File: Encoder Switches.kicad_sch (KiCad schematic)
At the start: 0 parts

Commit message: Added oled hierarchical page and referenced other pages
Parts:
- added C? (x27): 100nf, symbol Device:C_Small
- added R? (x27): 10k, Resistor_SMD:R_0201_0603Metric, symbol Device:R
- added SW?: Encoder4, ksoloti_shield_footprints:ALPS_STEC12E08, symbol ksoloti_shield_symbols:RotaryEncoder_Switch_GND
- added SW?: Encoder3, ksoloti_shield_footprints:ALPS_STEC12E08, symbol ksoloti_shield_symbols:RotaryEncoder_Switch_GND
- added SW?: Encoder1, ksoloti_shield_footprints:ALPS_STEC12E08, symbol ksoloti_shield_symbols:RotaryEncoder_Switch_GND
- added SW?: Encoder7, ksoloti_shield_footprints:ALPS_STEC12E08, symbol ksoloti_shield_symbols:RotaryEncoder_Switch_GND
- added SW?: Encoder5, ksoloti_shield_footprints:ALPS_STEC12E08, symbol ksoloti_shield_symbols:RotaryEncoder_Switch_GND
- added SW?: Encoder8, ksoloti_shield_footprints:ALPS_STEC12E08, symbol ksoloti_shield_symbols:RotaryEncoder_Switch_GND
- added SW?: Encoder9, ksoloti_shield_footprints:ALPS_STEC12E08, symbol ksoloti_shield_symbols:RotaryEncoder_Switch_GND
- added SW?: Encoder6, ksoloti_shield_footprints:ALPS_STEC12E08, symbol ksoloti_shield_symbols:RotaryEncoder_Switch_GND
- added SW?: Encoder2, ksoloti_shield_footprints:ALPS_STEC12E08, symbol ksoloti_shield_symbols:RotaryEncoder_Switch_GND
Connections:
- new net: C?.1, R?.2, SW?.A (x9)
- new net +3.3V: R?.1, R?.1, R?.1, R?.1, R?.1, R?.1, R?.1, R?.1, R?.1, R?.1, R?.1, R?.1, R?.1, R?.1, R?.1, R?.1, R?.1, R?.1, R?.2, R?.2, R?.2, R?.2, R?.2, R?.2, R?.2, R?.2, R?.2
- new net ENC1_B: C?.1, R?.2, SW?.B
- new net ENC1_SW: C?.1, R?.1, SW?.S2
- new net ENC2_B: C?.1, R?.2, SW?.B
- new net ENC2_SW: C?.1, R?.1, SW?.S2
- new net ENC3_B: C?.1, R?.2, SW?.B
- new net ENC3_SW: C?.1, C?.1, R?.1, R?.1, SW?.S2, SW?.S2
- new net ENC4_B: C?.1, R?.2, SW?.B
- new net ENC4_SW: C?.1, R?.1, SW?.S2
- new net ENC5_B: C?.1, R?.2, SW?.B
- new net ENC5_SW: C?.1, R?.1, SW?.S2
- new net ENC6_B: C?.1, R?.2, SW?.B
- new net ENC6_SW: C?.1, R?.1, SW?.S2
- new net ENC7_B: C?.1, R?.2, SW?.B
- new net ENC8_B: C?.1, R?.2, SW?.B
- new net ENC8_SW: C?.1, R?.1, SW?.S2
- new net ENC9_B: C?.1, R?.2, SW?.B
- new net ENC9_SW: C?.1, R?.1, SW?.S2
- new net GND: C?.2, C?.2, C?.2, C?.2, C?.2, C?.2, C?.2, C?.2, C?.2, C?.2, C?.2, C?.2, C?.2, C?.2, C?.2, C?.2, C?.2, C?.2, C?.2, C?.2, C?.2, C?.2, C?.2, C?.2, C?.2, C?.2, C?.2, SW?.1, SW?.1, SW?.1, SW?.1, SW?.1, SW?.1, SW?.1, SW?.1, SW?.1, SW?.C, SW?.C, SW?.C, SW?.C, SW?.C, SW?.C, SW?.C, SW?.C, SW?.C, SW?.S1, SW?.S1, SW?.S1, SW?.S1, SW?.S1, SW?.S1, SW?.S1, SW?.S1, SW?.S1

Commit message: Annotated all components (numerating)
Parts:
- gave numbers to parts that had none: 63

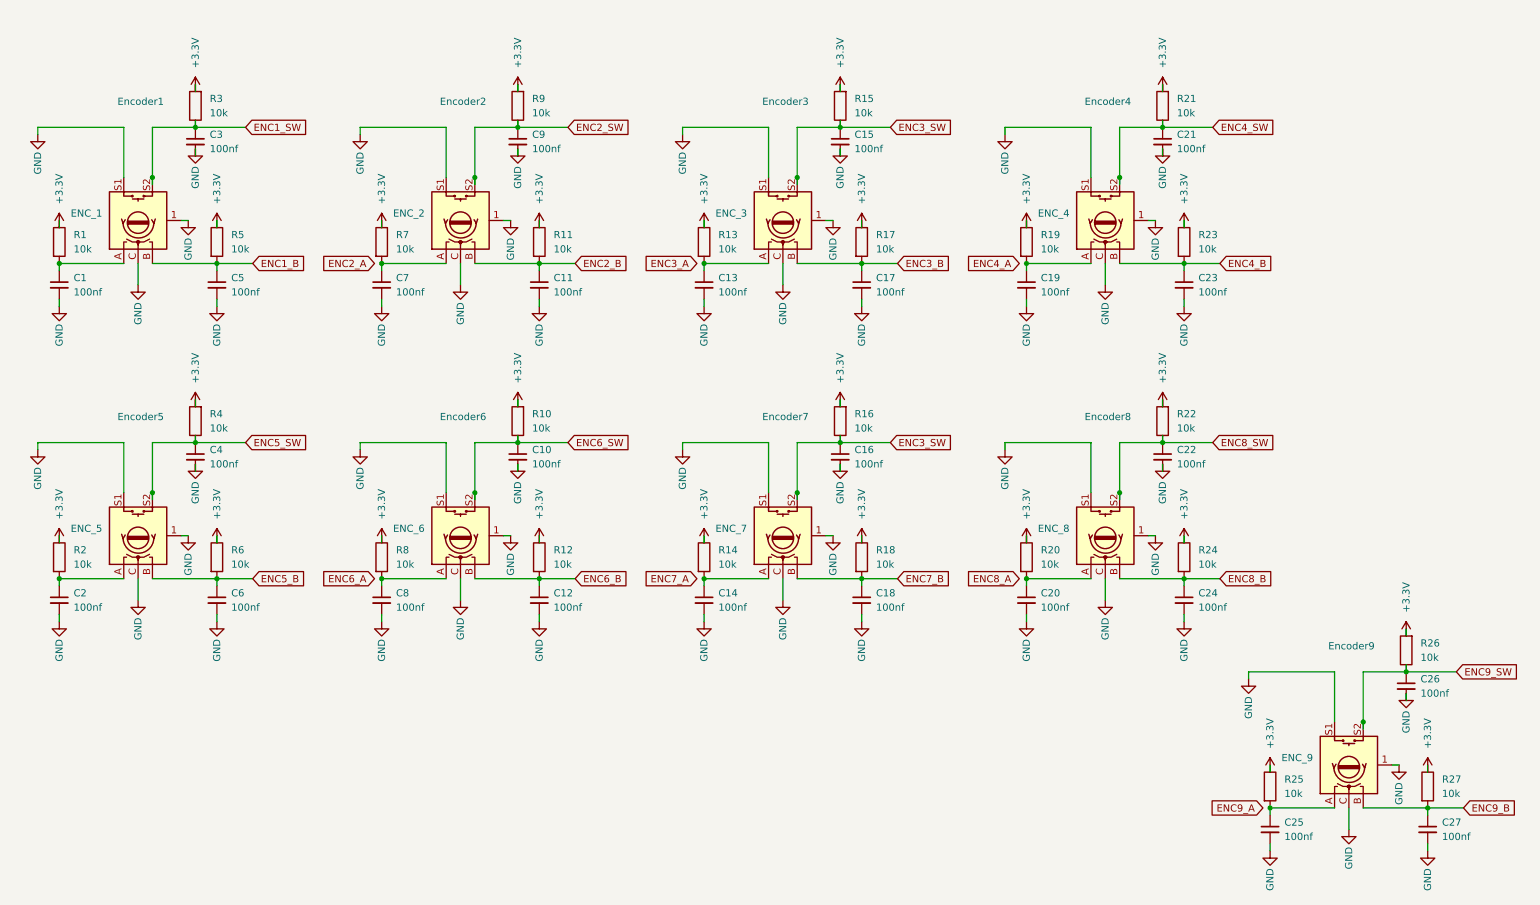
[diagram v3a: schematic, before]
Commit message: Cleaned up ERC errors
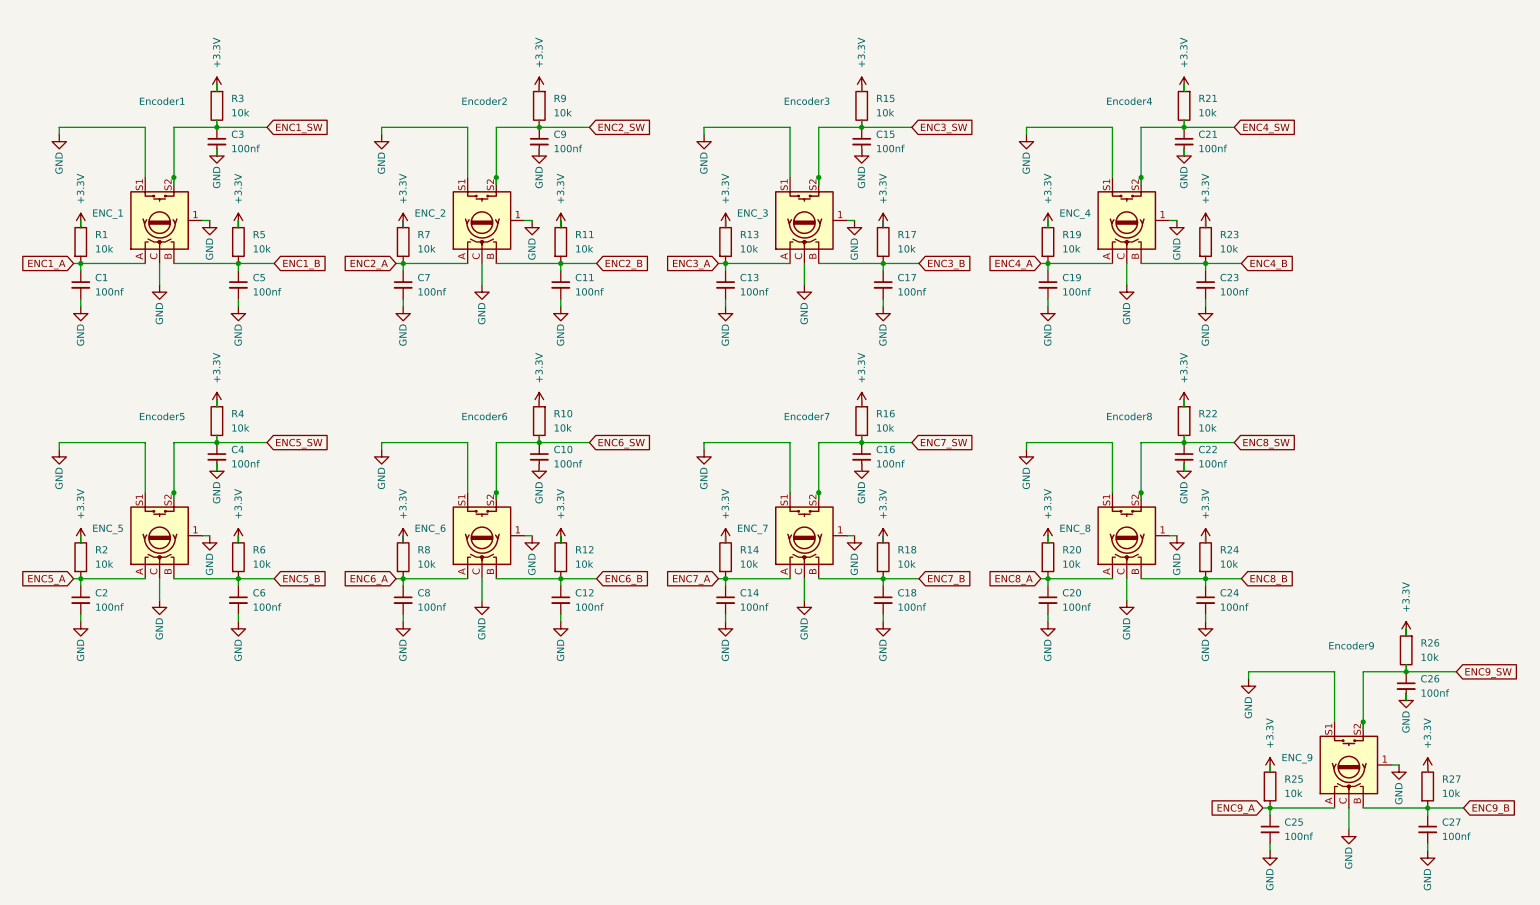
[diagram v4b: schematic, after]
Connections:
- net ENC2_A: now also C7.1, ENC_2.A, R7.2
- net ENC3_A: now also C13.1, ENC_3.A, R13.2
- net ENC3_SW: no longer C16.1, ENC_7.S2, R16.1
- net ENC4_A: now also C19.1, ENC_4.A, R19.2
- net ENC6_A: now also C8.1, ENC_6.A, R8.2
- net ENC7_A: now also C14.1, ENC_7.A, R14.2
- net ENC8_A: now also C20.1, ENC_8.A, R20.2
- net ENC9_A: now also C25.1, ENC_9.A, R25.2
- net ENC5_A: now reaches C2.1, ENC_5.A, R2.2
- net ENC1_A: now reaches C1.1, ENC_1.A, R1.2
- new net ENC7_SW: C16.1, ENC_7.S2, R16.1
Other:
- moved on the sheet: C1, C10, C11, C12, C13, C14, C15, C16, C17, C18, C19, C2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

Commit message: Solve all warnings
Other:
- moved on the sheet: R10, R15, R16, R21, R22, R26, R3, R4, R9

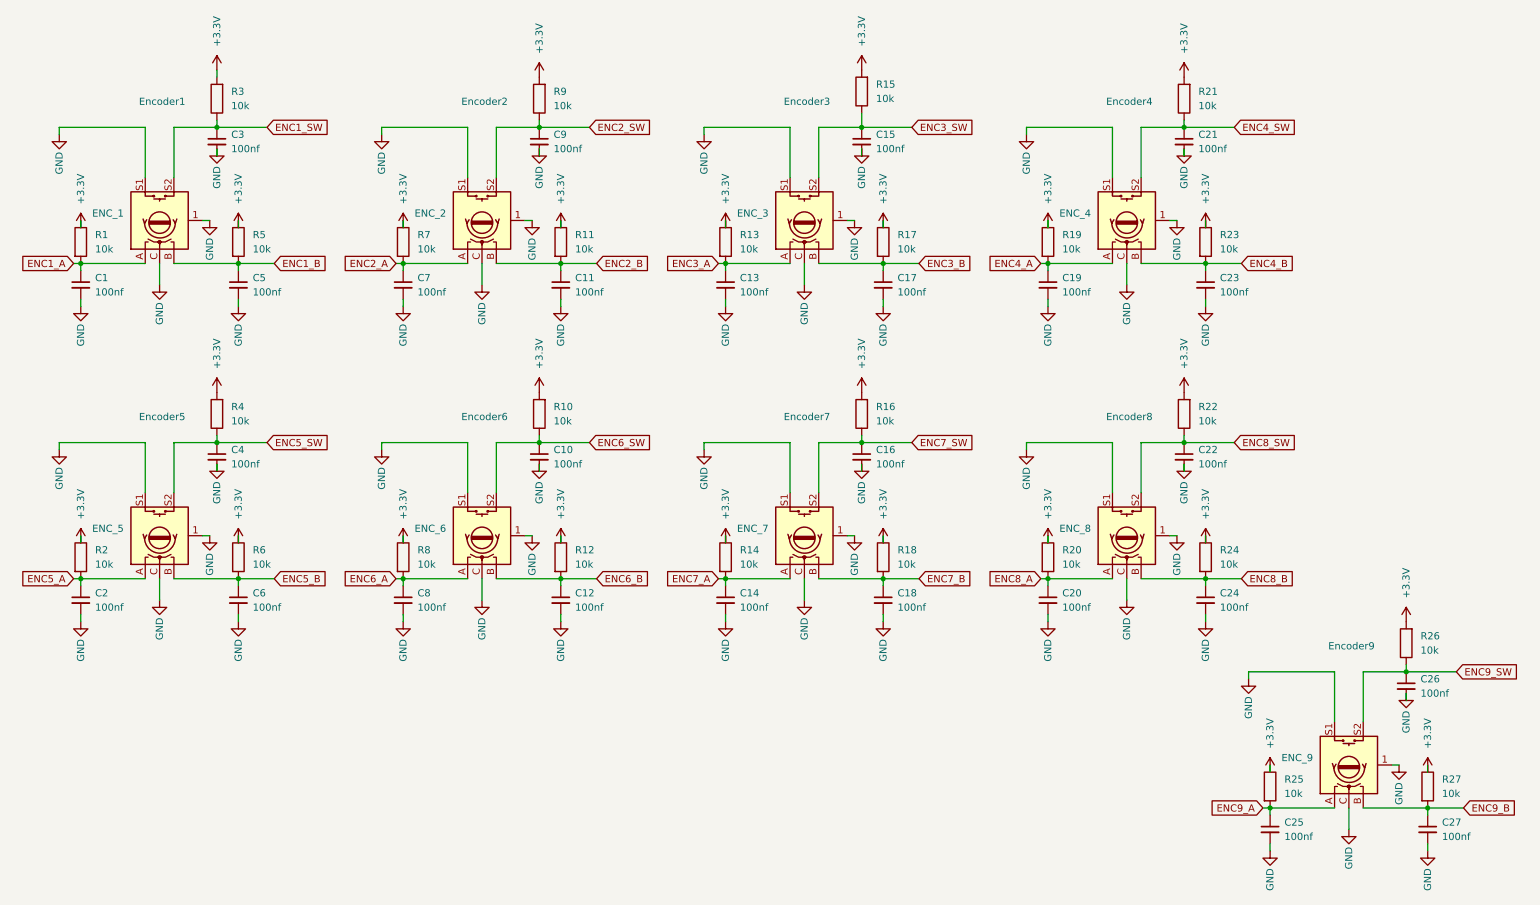
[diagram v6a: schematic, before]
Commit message: Removed final warnings
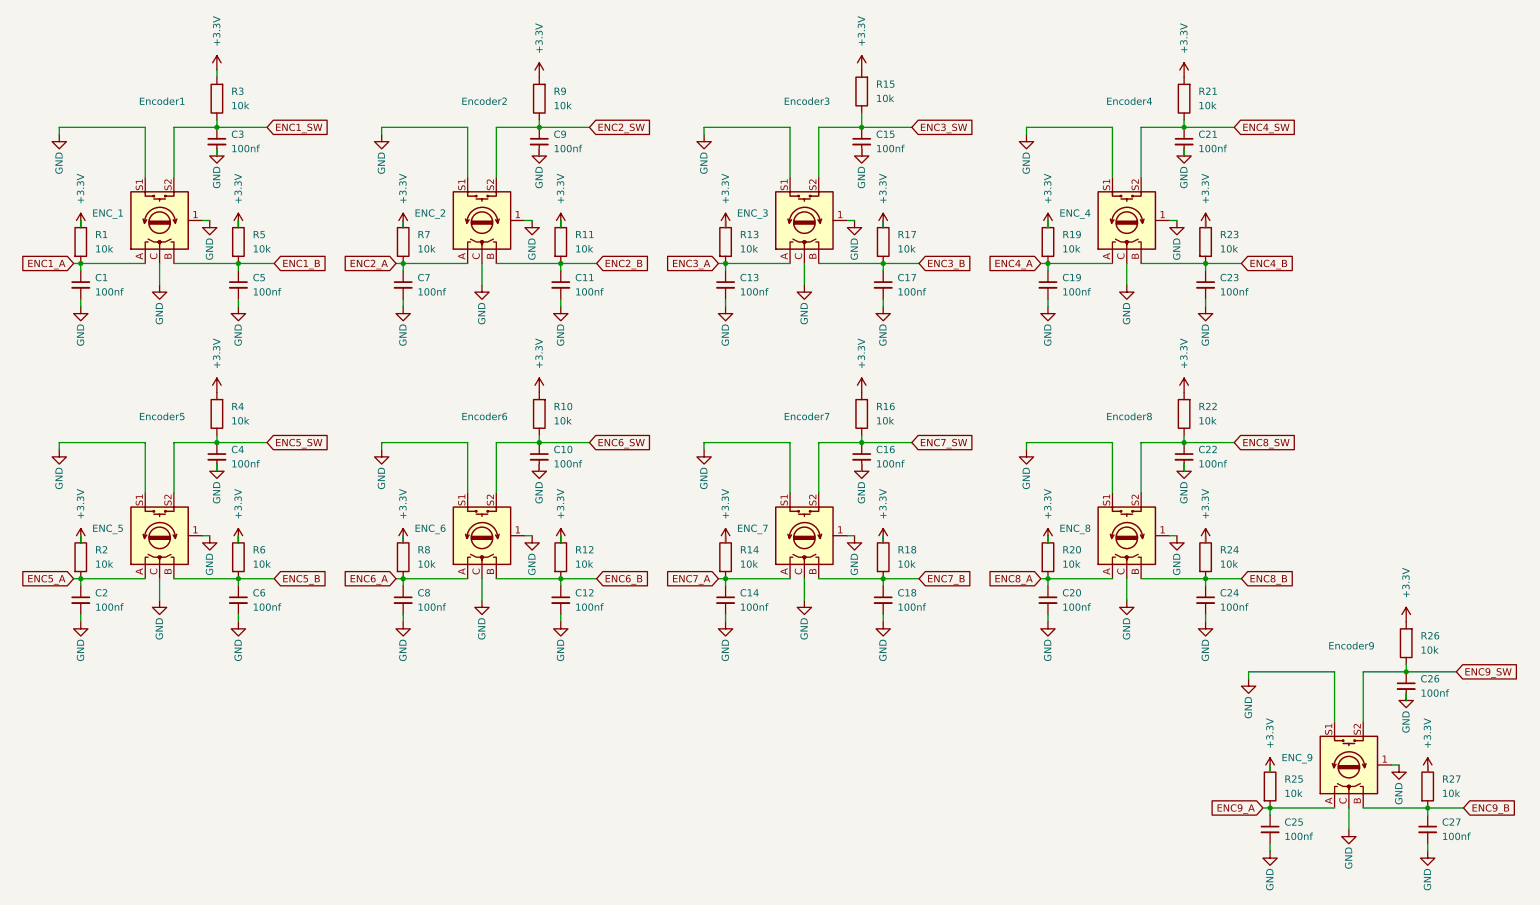
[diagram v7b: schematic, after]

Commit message: Added jack symbols and footprints also footprints for ics and caps
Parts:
- C1, C10, C11, C12, C13, C14, C15, C16, C17, C18, C19, C2, C20, C21, C22, C23, C24, C25, C26, C27, C3, C4, C5, C6, C7, C8, C9: footprint (none) -> Capacitor_SMD:C_0603_1608Metric
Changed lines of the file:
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@@
 			)
 		)
-		(property "Footprint" ""
+		(property "Footprint" "Capacitor_SMD:C_0603_1608Metric"
 			(at 24.13 113.03 0)
 			(effects
@@
 			)
 		)
-		(property "Footprint" ""
+		(property "Footprint" "Capacitor_SMD:C_0603_1608Metric"
 			(at 219.71 87.63 0)
 			(effects
@@
 			)
 		)
-		(property "Footprint" ""
+		(property "Footprint" "Capacitor_SMD:C_0603_1608Metric"
 			(at 259.08 128.27 0)
 			(effects
@@
 			)
 		)
-		(property "Footprint" ""
+		(property "Footprint" "Capacitor_SMD:C_0603_1608Metric"
 			(at 48.26 87.63 0)
 			(effects
@@
 			)
 		)
-		(property "Footprint" ""
+		(property "Footprint" "Capacitor_SMD:C_0603_1608Metric"
 			(at 223.52 57.15 0)
 			(effects
@@
 			)
 		)
-		(property "Footprint" ""
+		(property "Footprint" "Capacitor_SMD:C_0603_1608Metric"
 			(at 138.43 113.03 0)
 			(effects
@@
 			)
 		)
-		(property "Footprint" ""
+		(property "Footprint" "Capacitor_SMD:C_0603_1608Metric"
 			(at 162.56 31.75 0)
 			(effects
@@
 			)
 		)
-		(property "Footprint" ""
+		(property "Footprint" "Capacitor_SMD:C_0603_1608Metric"
 			(at 223.52 113.03 0)
 			(effects
@@
 			)
 		)
-		(property "Footprint" ""
+		(property "Footprint" "Capacitor_SMD:C_0603_1608Metric"
 			(at 109.22 113.03 0)
 			(effects
@@
 			)
 		)
-		(property "Footprint" ""
+		(property "Footprint" "Capacitor_SMD:C_0603_1608Metric"
 			(at 109.22 57.15 0)
 			(effects
@@
 			)
 		)
-		(property "Footprint" ""
+		(property "Footprint" "Capacitor_SMD:C_0603_1608Metric"
 			(at 81.28 113.03 0)
 			(effects
@@
 			)
 		)
-		(property "Footprint" ""
+		(property "Footprint" "Capacitor_SMD:C_0603_1608Metric"
 			(at 162.56 87.63 0)
 			(effects
@@
 			)
 		)
-		(property "Footprint" ""
+		(property "Footprint" "Capacitor_SMD:C_0603_1608Metric"
 			(at 166.37 57.15 0)
 			(effects
@@
 			)
 		)
-		(property "Footprint" ""
+		(property "Footprint" "Capacitor_SMD:C_0603_1608Metric"
 			(at 52.07 57.15 0)
 			(effects
@@
 			)
 		)
-		(property "Footprint" ""
+		(property "Footprint" "Capacitor_SMD:C_0603_1608Metric"
 			(at 24.13 57.15 0)
 			(effects
@@
 			)
 		)
-		(property "Footprint" ""
+		(property "Footprint" "Capacitor_SMD:C_0603_1608Metric"
 			(at 195.58 57.15 0)
 			(effects
@@
 			)
 		)
-		(property "Footprint" ""
+		(property "Footprint" "Capacitor_SMD:C_0603_1608Metric"
 			(at 105.41 31.75 0)
 			(effects
@@
 			)
 		)
-		(property "Footprint" ""
+		(property "Footprint" "Capacitor_SMD:C_0603_1608Metric"
 			(at 262.89 153.67 0)
 			(effects
@@
 			)
 		)
-		(property "Footprint" ""
+		(property "Footprint" "Capacitor_SMD:C_0603_1608Metric"
 			(at 166.37 113.03 0)
 			(effects
@@
 			)
 		)
-		(property "Footprint" ""
+		(property "Footprint" "Capacitor_SMD:C_0603_1608Metric"
 			(at 219.71 31.75 0)
 			(effects
@@
 			)
 		)
-		(property "Footprint" ""
+		(property "Footprint" "Capacitor_SMD:C_0603_1608Metric"
 			(at 52.07 113.03 0)
 			(effects
@@
 			)
 		)
-		(property "Footprint" ""
+		(property "Footprint" "Capacitor_SMD:C_0603_1608Metric"
 			(at 48.26 31.75 0)
 			(effects
@@
 			)
 		)
-		(property "Footprint" ""
+		(property "Footprint" "Capacitor_SMD:C_0603_1608Metric"
 			(at 234.95 153.67 0)
 			(effects
@@
 			)
 		)
-		(property "Footprint" ""
+		(property "Footprint" "Capacitor_SMD:C_0603_1608Metric"
 			(at 81.28 57.15 0)
 			(effects
@@
 			)
 		)
-		(property "Footprint" ""
+		(property "Footprint" "Capacitor_SMD:C_0603_1608Metric"
 			(at 105.41 87.63 0)
 			(effects
@@
 			)
 		)
-		(property "Footprint" ""
+		(property "Footprint" "Capacitor_SMD:C_0603_1608Metric"
 			(at 195.58 113.03 0)
 			(effects
@@
 			)
 		)
-		(property "Footprint" ""
+		(property "Footprint" "Capacitor_SMD:C_0603_1608Metric"
 			(at 138.43 57.15 0)
 			(effects
